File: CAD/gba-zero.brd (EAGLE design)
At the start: 130.7 x 72.9 mm, 59 parts, among them J1 SWTCHCRFT_3.5JACK5-JACK-SMD, P1 50_PIN_CON, P3 LINK_CONNECTOR, Q1 BSS138, U1 APX803, U2 NC7WZ16, U3 74LVC2G02, U4 74LVC3G04, U5 LM4875, U6 RPI-ZEROSMD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

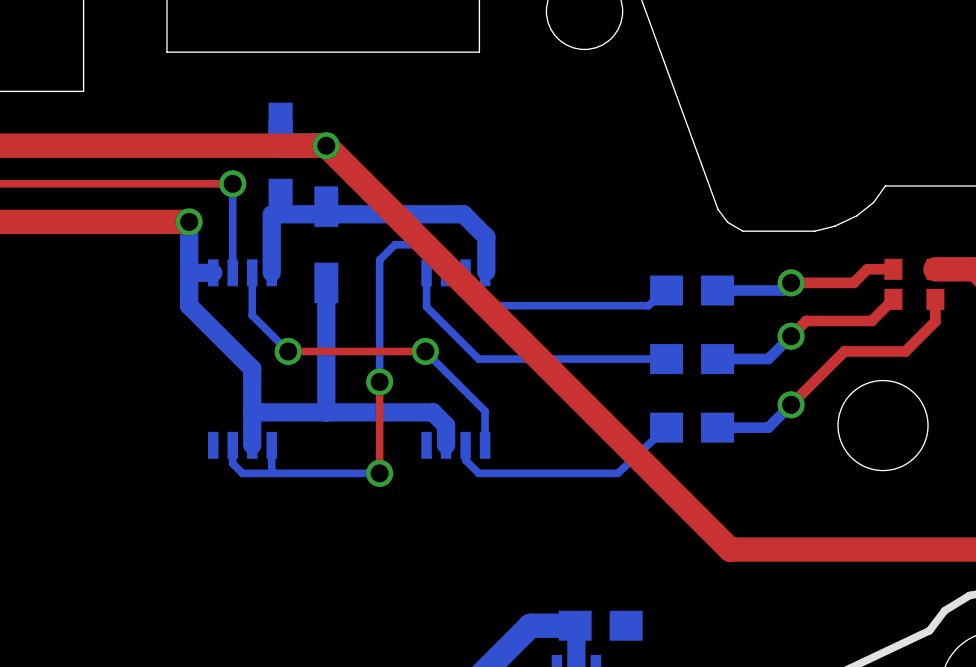
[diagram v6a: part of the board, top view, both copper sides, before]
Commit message: Fixed TSSOP-8 package
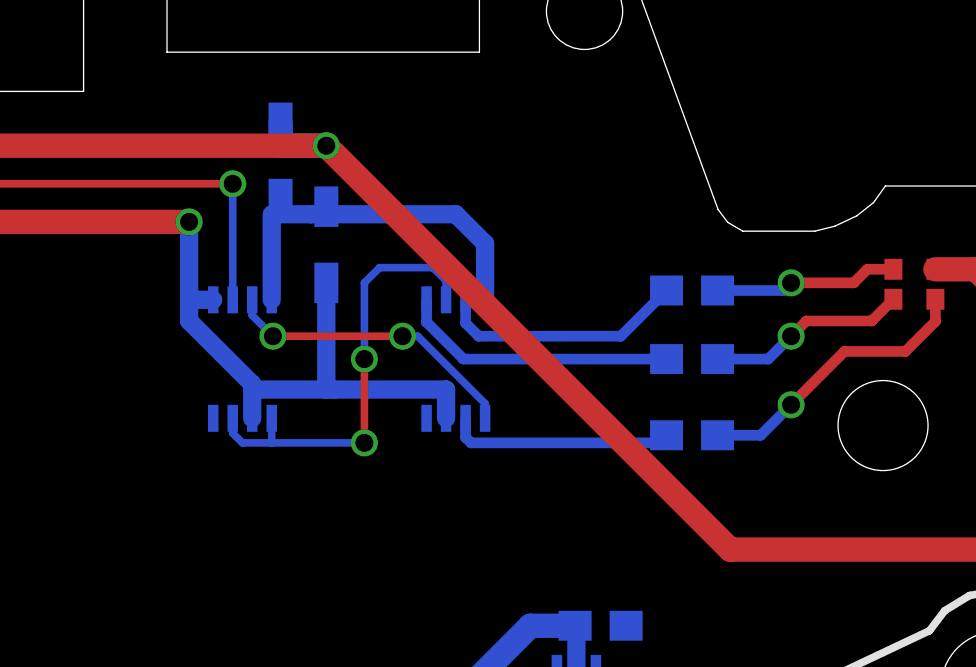
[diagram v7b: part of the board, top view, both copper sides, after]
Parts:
- moved R16 0.25 mm to (105.7, 56.4)
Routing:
- net N$16: track 17.1 -> 14.9 mm
- net N$15: track 11.6 -> 9.99 mm
- net N$19: track 11.4 -> 13.0 mm
- net USB: track 69.5 -> 67.9 mm
- net LBO: track 56.5 -> 57.4 mm
- net N$11: track 9.86 -> 9.25 mm
- net N$13: track 7.72 -> 8.29 mm

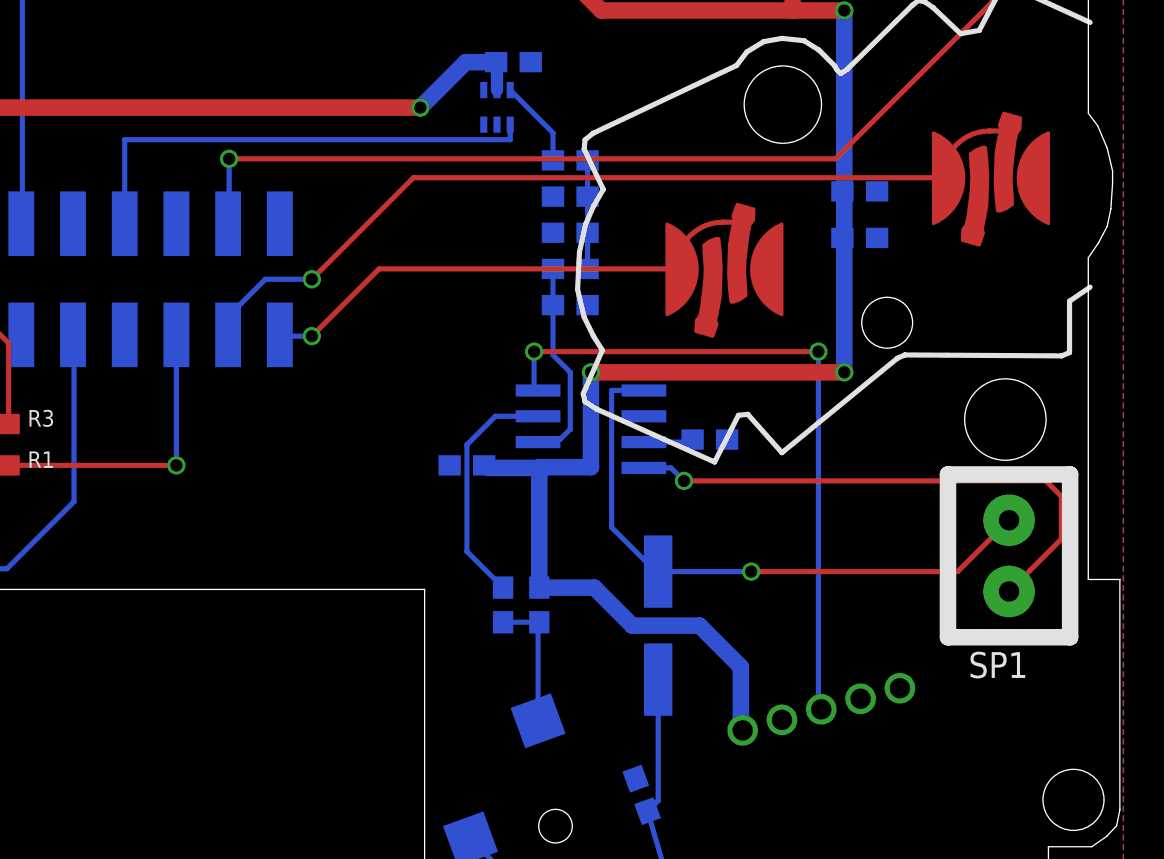
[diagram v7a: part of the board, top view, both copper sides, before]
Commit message: Swapped VCC & GND for the volume dial
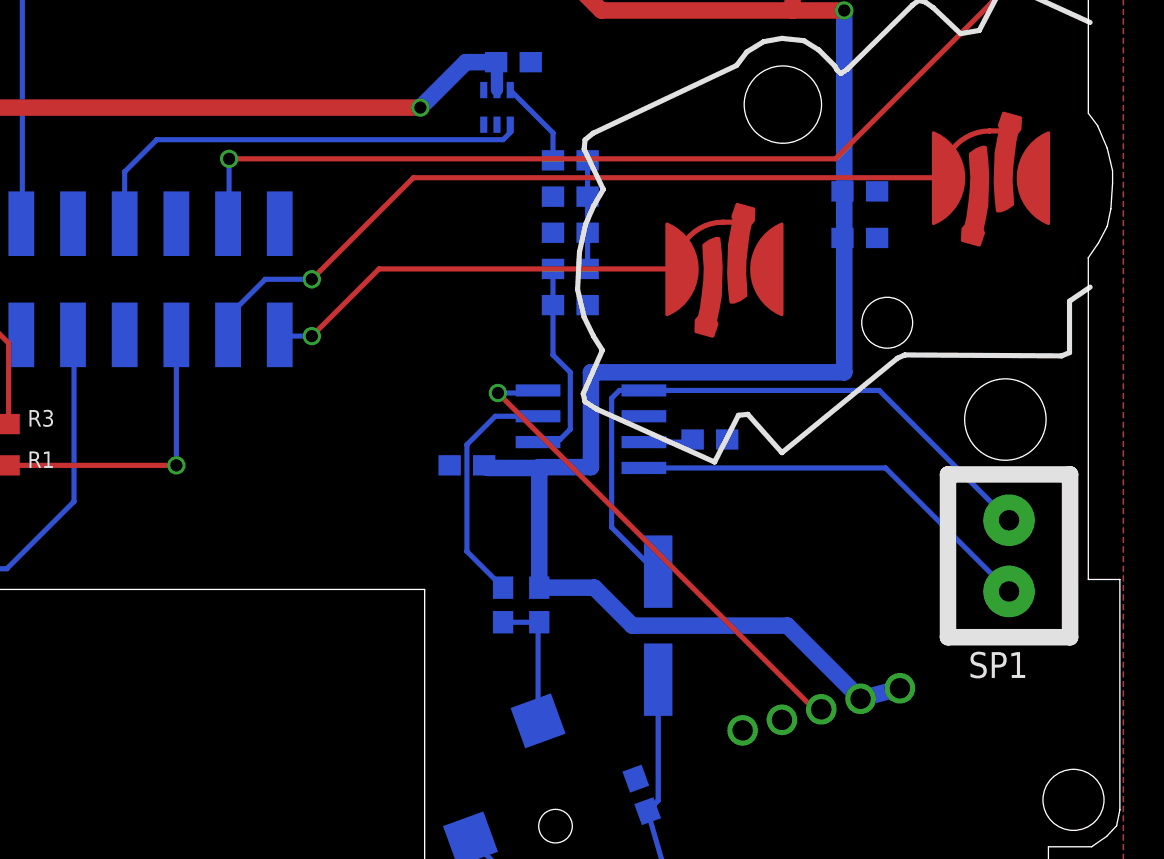
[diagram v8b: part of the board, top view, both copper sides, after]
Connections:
- net +5V: now also R17.3, R17.3O; no longer R17.1
- net GND: now also R17.1; no longer R17.3, R17.3O
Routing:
- net VOL/SD: track 33.7 -> 24.4 mm, vias 2 -> 1
- net VO2: track 26.8 -> 20.5 mm, vias 1 -> 0
- net +5V: track 227.6 -> 233.0 mm, vias 6 -> 4
- net VO1: track 29.8 -> 31.9 mm, vias 1 -> 0
- net AUD_PWM: track 23.8 -> 22.7 mm
